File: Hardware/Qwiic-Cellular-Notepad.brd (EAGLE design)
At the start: 45.7 x 59.7 mm, 119 parts, among them J10 U.FL, J12 U.FL, J14 I2C, J15 SIM Socket, J3 QWIIC_RIGHT_ANGLE, J6 External SIM, J8 QWIIC_RIGHT_ANGLE, U2 MCP73831, U4 BLUES NOTECARD

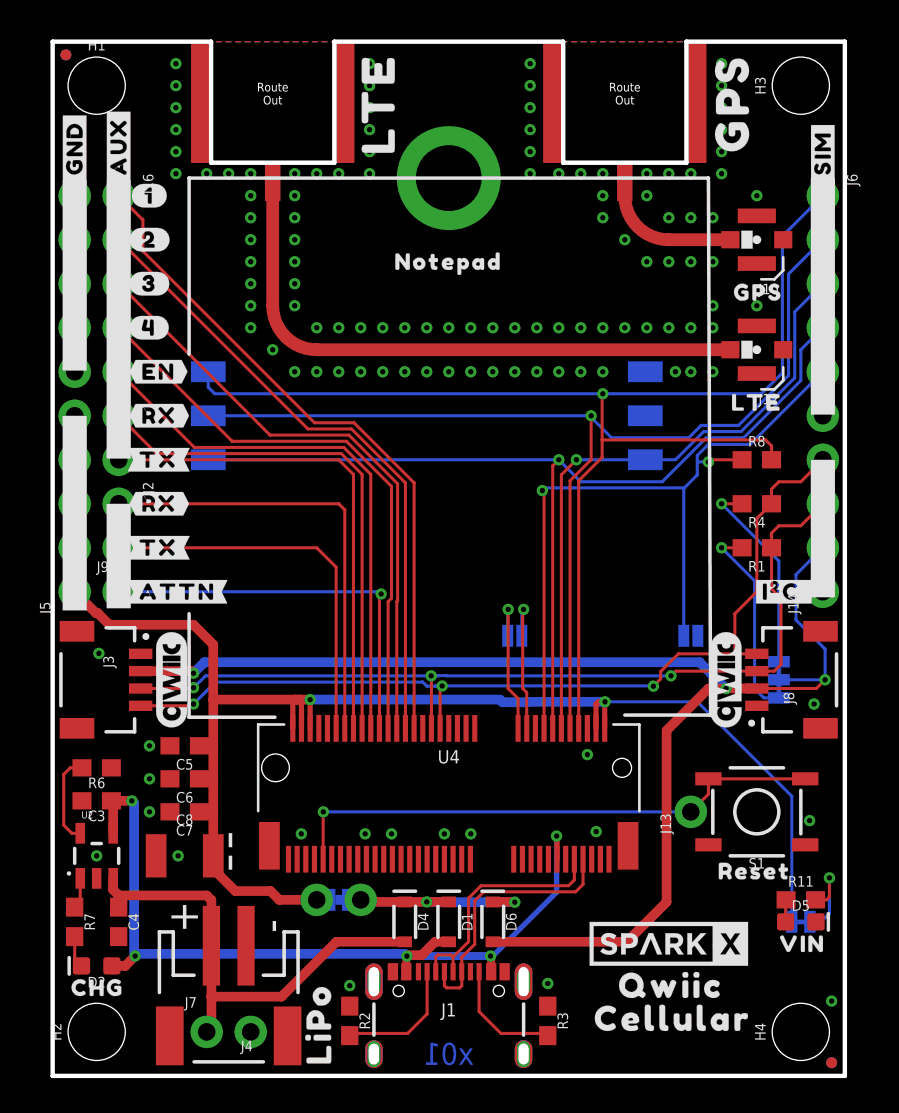
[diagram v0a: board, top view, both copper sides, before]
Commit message: Fix Notecard FP. Add VIO vreg. x02 release.
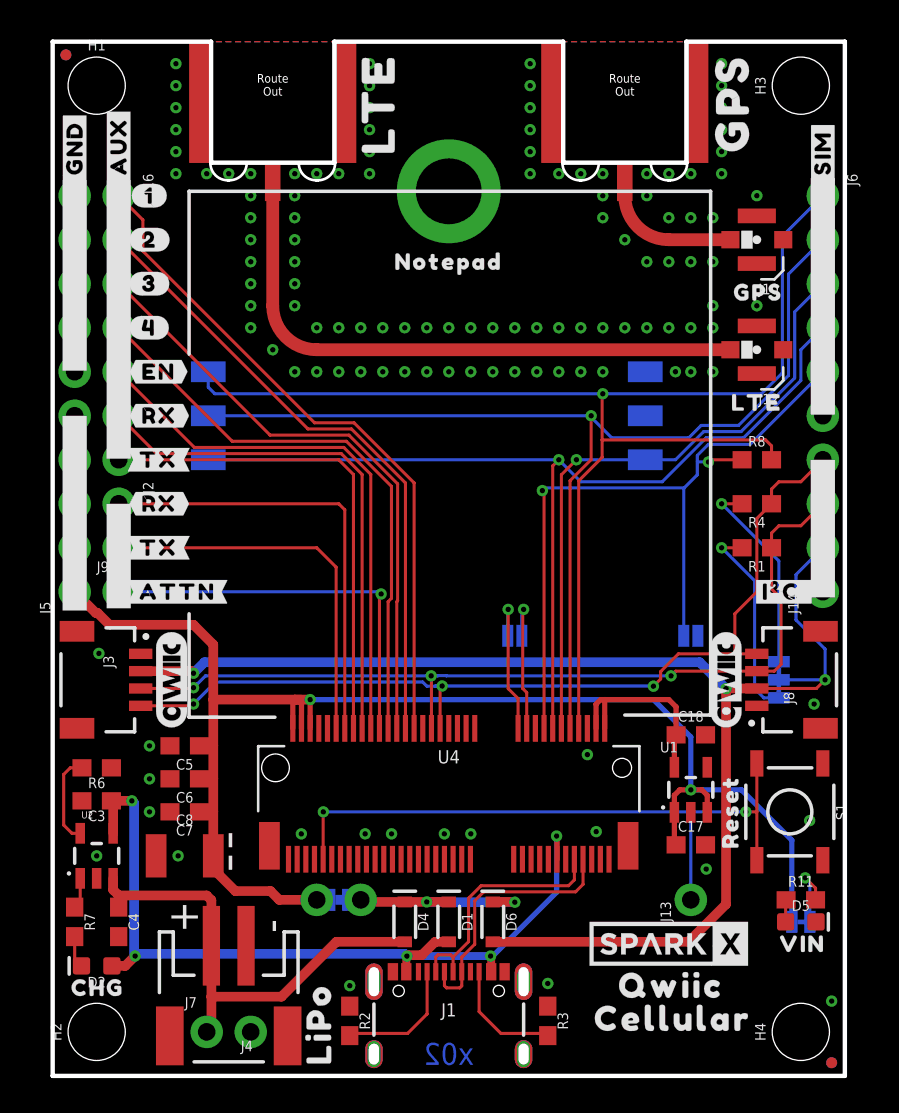
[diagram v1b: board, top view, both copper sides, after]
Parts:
- added C17, C18: 1.0uF, SparkFun-Capacitors:0603
- added U1: STLQ015-3.3V, SparkFun-IC-Power:SOT23-5
- E3, E4: value (none) -> SMA
- H5: value STAND-OFF-REFLOW2.5MM_TALL -> STAND-OFF
- moved J13 5.08 mm to (36.8, 10.2)
- moved U$30 5.08 mm to (36.2, 10.2)
- moved S1 1.91 mm to (42.5, 15.2), turned to 270 degrees
- moved U$92 1.53 mm to (39.1, 12.4), turned to 90 degrees
- moved H5 0.76 mm to (22.9, 51.1)
- renumbered E1 to E4, E2 to E3
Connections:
- new net VIO: C18.1, U1.5, U4.2, U4.4
- net GND: now also C17.2, C18.2, U1.2
- net VIN: now also C17.1, U1.1, U1.3; no longer U4.2, U4.4
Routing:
- net VIO: track 0.00 -> 11.5 mm
- net !RESET!: track 31.9 -> 38.4 mm, vias 1 -> 2
- net VIN: track 94.1 -> 97.0 mm
- net 3.3V: track 77.6 -> 79.1 mm
- net N$6: track 5.35 -> 4.17 mm
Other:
- board text added: "x02"
- board text removed: "x01"

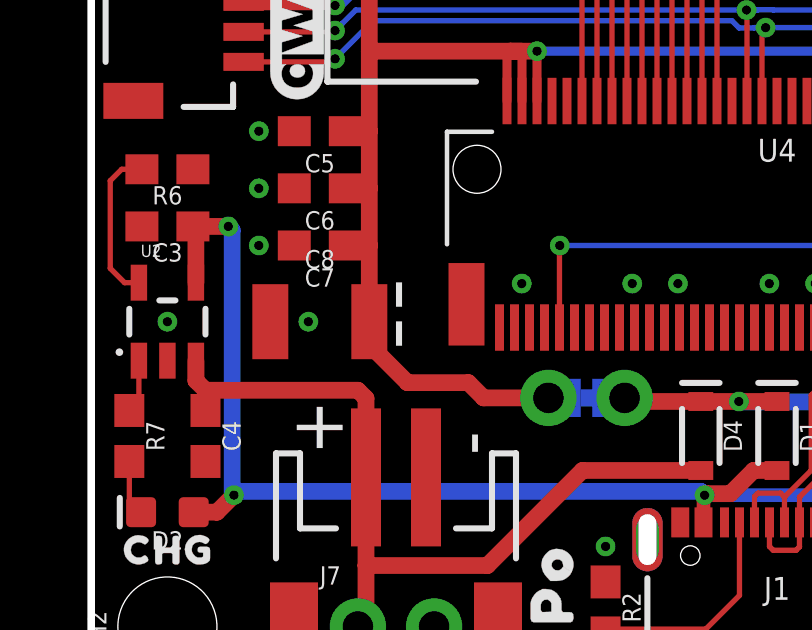
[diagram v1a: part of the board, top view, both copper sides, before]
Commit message: Change to 22uF cap. Add production files.
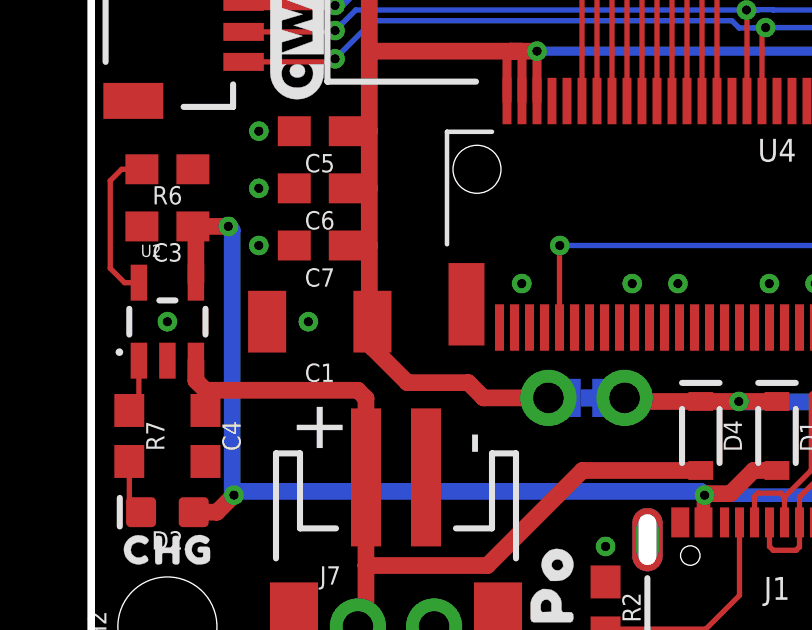
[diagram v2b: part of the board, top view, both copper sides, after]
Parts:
- removed C8: 68uF, SparkFun-Capacitors:EIA3528
- added C1: 22uF, SparkFun-Capacitors:1210
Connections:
- net GND: now also C1.2; no longer C8.C
- net VIN: now also C1.1; no longer C8.A
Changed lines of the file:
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@@
 <attribute name="VALUE" x="1.778" y="52.07" size="0.6096" layer="27" font="vector" ratio="20" rot="R270"/>
-</element>
-<element name="C8" library="SparkFun-Capacitors" package="EIA3528" value="68uF" x="7.62" y="12.7" smashed="yes">
-<attribute name="NAME" x="7.62" y="14.478" size="0.6096" layer="25" font="vector" ratio="20" align="bottom-center"/>
-<attribute name="PROD_ID" value="CAP-10790" x="7.62" y="12.7" size="1.778" layer="27" font="vector" ratio="15" display="off"/>
-<attribute name="VALUE" x="7.62" y="10.922" size="0.6096" layer="27" font="vector" ratio="20" align="top-center"/>
 </element>
 <element name="J2" library="SparkFun-Connectors" package="1X02_NO_SILK" value="" x="3.81" y="33.02" smashed="yes" rot="R270">
@@
 <attribute name="PROD_ID" value="CAP-13930" x="29.21" y="22.225" size="1.778" layer="27" font="vector" ratio="15" display="off"/>
 <attribute name="VALUE" x="36.83" y="18.923" size="0.6096" layer="27" font="vector" ratio="20" align="top-center"/>
+</element>
+<element name="C1" library="SparkFun-Capacitors" package="1210" value="22uF" x="7.62" y="12.7" smashed="yes" rot="R180">
+<attribute name="NAME" x="7.62" y="11.303" size="0.6096" layer="25" font="vector" ratio="20" rot="R180" align="bottom-center"/>
+<attribute name="PROD_ID" value="CAP-10381" x="7.62" y="12.7" size="1.778" layer="27" font="vector" ratio="15" rot="R180" display="off"/>
+<attribute name="VALUE" x="7.62" y="14.097" size="0.6096" layer="27" font="vector" ratio="20" rot="R180" align="top-center"/>
 </element>
 </elements>
@@
 <contactref element="J5" pad="10"/>
 <contactref element="J5" pad="6"/>
-<contactref element="C8" pad="C"/>
 <via x="2.54" y="12.7" extent="1-16" drill="0.3048"/>
 <via x="7.239" y="12.7" extent="1-16" drill="0.3048"/>
@@
 <contactref element="C17" pad="2"/>
 <via x="37.719" y="11.938" extent="1-16" drill="0.3048"/>
+<contactref element="C1" pad="2"/>
 </signal>
 <signal name="3.3V">
@@
 <contactref element="J5" pad="4"/>
 <contactref element="J5" pad="5"/>
-<contactref element="C8" pad="A"/>
 <wire x1="15.24" y1="10.16" x2="13.081" y2="10.16" width="0.5588" layer="1"/>
-<wire x1="12.573" y1="10.668" x2="10.541" y2="10.668" width="0.5588" layer="1"/>
-<wire x1="9.27" y1="11.939" x2="9.27" y2="12.7" width="0.5588" layer="1"/>
+<wire x1="10.541" y1="10.668" x2="12.573" y2="10.668" width="0.5588" layer="1"/>
 <wire x1="13.081" y1="10.16" x2="12.573" y2="10.668" width="0.5588" layer="1"/>
-<wire x1="10.541" y1="10.668" x2="9.27" y2="11.939" width="0.5588" layer="1"/>
-<wire x1="9.27" y1="12.7" x2="9.27" y2="15.24" width="0.5588" layer="1"/>
 <wire x1="9.27" y1="15.24" x2="9.27" y2="17.145" width="0.5588" layer="1"/>
 <wire x1="9.27" y1="17.145" x2="9.27" y2="19.05" width="0.5588" layer="1"/>
@@
 <wire x1="37.465" y1="16.51" x2="36.83" y2="16.51" width="0.3048" layer="1"/>
 <wire x1="37.78" y1="16.195" x2="37.465" y2="16.51" width="0.3048" layer="1"/>
+<contactref element="C1" pad="1"/>
+<wire x1="9.27" y1="15.24" x2="9.271" y2="15.239" width="0.5588" layer="1"/>
+<wire x1="9.271" y1="12.804" x2="9.375" y2="12.7" width="0.5588" layer="1"/>
+<wire x1="9.271" y1="15.239" x2="9.271" y2="12.804" width="0.5588" layer="1"/>
+<wire x1="9.375" y1="12.7" x2="9.375" y2="11.834" width="0.5588" layer="1"/>
+<wire x1="9.375" y1="11.834" x2="10.541" y2="10.668" width="0.5588" layer="1"/>
 </signal>
 <signal name="N$7">

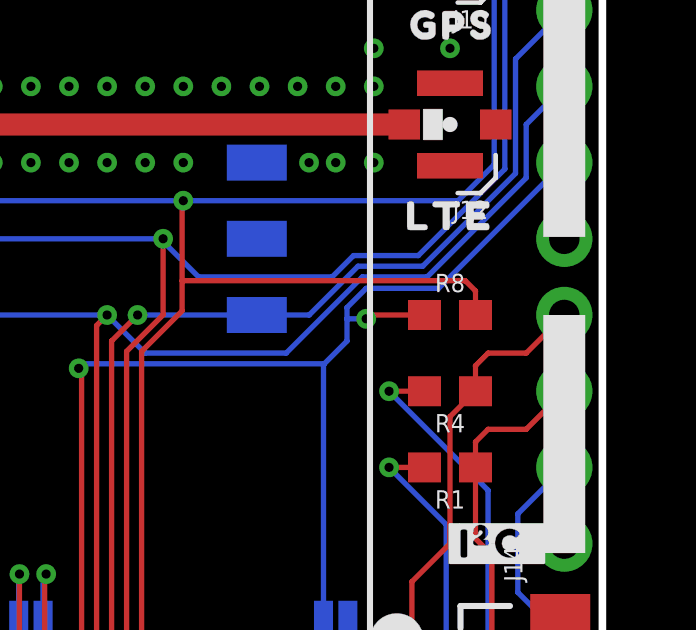
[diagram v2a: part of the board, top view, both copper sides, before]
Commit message: Change R8 to DNP.
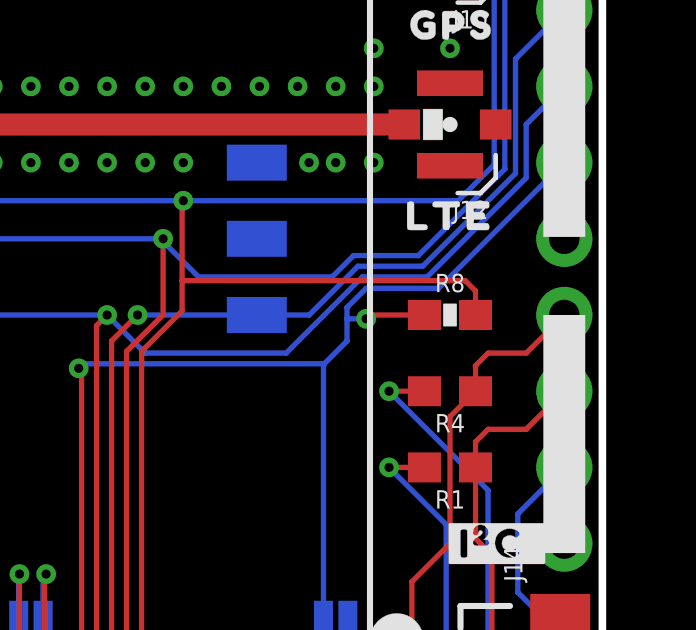
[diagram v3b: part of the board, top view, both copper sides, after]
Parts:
- R8: value 10k -> DNP; device SparkFun-Resistors:0603 -> Testing:0603-RES
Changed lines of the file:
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@@
 <attribute name="VALUE" x="42.418" y="52.07" size="0.6096" layer="27" font="vector" ratio="20" rot="R270"/>
 </element>
-<element name="R8" library="SparkFun-Resistors" package="0603" value="10k" x="40.64" y="35.56" smashed="yes">
+<element name="R8" library="Testing" package="0603-RES" value="DNP" x="40.64" y="35.56" smashed="yes">
 <attribute name="NAME" x="40.64" y="36.322" size="0.6096" layer="25" font="vector" ratio="20" align="bottom-center"/>
-<attribute name="PROD_ID" value="RES-00824" x="40.64" y="35.56" size="1.778" layer="27" font="vector" ratio="15" display="off"/>
-<attribute name="VALUE" x="40.64" y="34.798" size="0.6096" layer="27" font="vector" ratio="20" align="top-center"/>
 </element>
 <element name="JP2" library="SparkFun-Jumpers" package="SMT-JUMPER_2_NO_SILK" package3d_urn="urn:adsk.eagle:package:39279/1" value="GPS_ANT_PWR" x="26.67" y="25.4" smashed="yes" rot="MR0">

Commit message: Add dimensionals
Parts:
- moved FRAME1 14.2 mm to (1.27, -24.1)
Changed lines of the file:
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@@
 <grid distance="0.05" unitdist="inch" unit="inch" style="lines" multiple="1" display="yes" altdistance="0.005" altunitdist="inch" altunit="inch"/>
 <layers>
-<layer number="1" name="Top" color="4" fill="1" visible="yes" active="yes"/>
-<layer number="16" name="Bottom" color="1" fill="1" visible="yes" active="yes"/>
+<layer number="1" name="Top" color="4" fill="1" visible="no" active="yes"/>
+<layer number="16" name="Bottom" color="1" fill="1" visible="no" active="yes"/>
 <layer number="17" name="Pads" color="2" fill="1" visible="yes" active="yes"/>
-<layer number="18" name="Vias" color="2" fill="1" visible="yes" active="yes"/>
-<layer number="19" name="Unrouted" color="6" fill="1" visible="yes" active="yes"/>
+<layer number="18" name="Vias" color="2" fill="1" visible="no" active="yes"/>
+<layer number="19" name="Unrouted" color="6" fill="1" visible="no" active="yes"/>
 <layer number="20" name="Dimension" color="24" fill="1" visible="yes" active="yes"/>
 <layer number="21" name="tPlace" color="16" fill="1" visible="yes" active="yes"/>
-<layer number="22" name="bPlace" color="14" fill="1" visible="yes" active="yes"/>
+<layer number="22" name="bPlace" color="14" fill="1" visible="no" active="yes"/>
 <layer number="23" name="tOrigins" color="15" fill="1" visible="yes" active="yes"/>
-<layer number="24" name="bOrigins" color="15" fill="1" visible="yes" active="yes"/>
+<layer number="24" name="bOrigins" color="15" fill="1" visible="no" active="yes"/>
 <layer number="25" name="tNames" color="7" fill="1" visible="no" active="yes"/>
 <layer number="26" name="bNames" color="7" fill="1" visible="no" active="yes"/>
-<layer number="27" name="tValues" color="7" fill="1" visible="no" active="yes"/>
+<layer number="27" name="tValues" color="7" fill="1" visible="yes" active="yes"/>
 <layer number="28" name="bValues" color="7" fill="1" visible="no" active="yes"/>
 <layer number="29" name="tStop" color="7" fill="3" visible="no" active="yes"/>
 <layer number="30" name="bStop" color="7" fill="6" visible="no" active="yes"/>
-<layer number="31" name="tCream" color="7" fill="4" visible="no" active="yes"/>
+<layer number="31" name="tCream" color="7" fill="4" visible="yes" active="yes"/>
 <layer number="32" name="bCream" color="7" fill="5" visible="no" active="yes"/>
 <layer number="33" name="tFinish" color="6" fill="3" visible="no" active="yes"/>
@@
 <layer number="45" name="Holes" color="7" fill="1" visible="yes" active="yes"/>
 <layer number="46" name="Milling" color="3" fill="1" visible="no" active="yes"/>
-<layer number="47" name="Measures" color="7" fill="1" visible="no" active="yes"/>
+<layer number="47" name="Measures" color="7" fill="1" visible="yes" active="yes"/>
 <layer number="48" name="Document" color="7" fill="1" visible="no" active="yes"/>
 <layer number="49" name="Reference" color="7" fill="1" visible="no" active="yes"/>
@@
 <text x="10.795" y="5.461" size="1.778" layer="22" ratio="15" rot="MR180">-</text>
 <text x="8.255" y="5.461" size="1.778" layer="22" ratio="15" rot="MR180">+</text>
-<text x="30.48" y="-10.16" size="1.778" layer="51" font="vector" ratio="15">N. Seidle</text>
-<wire x1="30.48" y1="41.91" x2="30.48" y2="-3.81" width="0.1016" layer="52"/>
+<text x="27.94" y="-24.13" size="1.778" layer="51" font="vector" ratio="15">N. Seidle</text>
 <rectangle x1="0.5715" y1="40.7035" x2="1.9685" y2="51.689" layer="22" rot="R180"/>
 <rectangle x1="0.5715" y1="26.8605" x2="1.9685" y2="38.1" layer="22" rot="R180"/>
@@
 <wire x1="29.464" y1="52.705" x2="36.576" y2="52.705" width="0.254" layer="20"/>
 <wire x1="36.576" y1="52.705" x2="36.576" y2="59.69" width="0.254" layer="20"/>
+<dimension x1="0" y1="0" x2="45.72" y2="0" x3="22.86" y3="-11.43" textsize="1.27" textratio="15" layer="47" unit="inch"/>
+<dimension x1="0" y1="0" x2="22.86" y2="0" x3="11.43" y3="-6.35" textsize="1.27" textratio="15" layer="47" unit="inch"/>
+<dimension x1="43.18" y1="2.54" x2="43.18" y2="57.15" x3="53.34" y3="29.845" textsize="1.27" textratio="15" layer="47" unit="inch"/>
+<dimension x1="43.18" y1="57.15" x2="2.54" y2="57.15" x3="22.86" y3="76.2" textsize="1.27" textratio="15" layer="47" unit="inch"/>
+<dimension x1="12.7" y1="59.69" x2="0" y2="59.69" x3="6.35" y3="67.31" textsize="1.27" textratio="15" layer="47" unit="inch"/>
+<dimension x1="12.7" y1="59.69" x2="33.02" y2="59.69" x3="22.86" y3="67.31" textsize="1.27" textratio="15" layer="47" unit="inch"/>
+<dimension x1="45.72" y1="59.69" x2="35.687" y2="65.659" x3="45.72" y3="62.6745" textsize="1.27" textratio="15" layer="47" dtype="vertical" unit="inch"/>
+<dimension x1="0" y1="0" x2="0" y2="22.86" x3="-11.43" y3="11.43" textsize="1.27" textratio="15" layer="47" dtype="vertical" unit="inch"/>
+<dimension x1="0" y1="0" x2="0" y2="2.54" x3="-2.54" y3="1.27" textsize="1.27" textratio="15" layer="47" dtype="vertical" unit="inch"/>
+<dimension x1="0" y1="0" x2="10.16" y2="0" x3="5.08" y3="-2.54" textsize="1.27" textratio="15" layer="47" dtype="vertical" unit="inch"/>
+<dimension x1="0" y1="0" x2="0" y2="59.69" x3="-17.78" y3="29.845" textsize="1.27" textratio="15" layer="47" dtype="vertical" unit="inch"/>
+<dimension x1="43.18" y1="2.54" x2="43.18" y2="0.889" x3="48.514" y3="1.7145" textsize="1.27" textratio="15" layer="47" dtype="vertical" unit="inch"/>
 </plain>
 <attributes>
@@
 </autorouter>
 <elements>
-<element name="FRAME1" library="SparkFun-Aesthetics" package="CREATIVE_COMMONS" value="FRAME-LEDGER" x="3.81" y="-10.16" smashed="yes">
-<attribute name="DESIGNER" value="" x="3.81" y="-10.16" size="1.778" layer="27" font="vector" ratio="15" display="off"/>
-<attribute name="REV" value="" x="3.81" y="-10.16" size="1.778" layer="27" font="vector" ratio="15" display="off"/>
+<element name="FRAME1" library="SparkFun-Aesthetics" package="CREATIVE_COMMONS" value="FRAME-LEDGER" x="1.27" y="-24.13" smashed="yes">
+<attribute name="DESIGNER" value="" x="1.27" y="-24.13" size="1.778" layer="27" font="vector" ratio="15" display="off"/>
+<attribute name="REV" value="" x="1.27" y="-24.13" size="1.778" layer="27" font="vector" ratio="15" display="off"/>
 </element>
 <element name="J1" library="SparkFun-Connectors" package="USB-C-16P-2LAYER-PADS" value="" x="22.86" y="6.35" smashed="yes">
